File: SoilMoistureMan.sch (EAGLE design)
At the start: 21 parts, among them Q1 BC847CSMD, Q2 BC857C, Q3 BC847CSMD, Q4 BC847CSMD, Q5 BC847CSMD

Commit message: schematic and Routing changes
schematic and Routing changes still WIP
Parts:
- added BAT2: 2032, kzh20_lithium_batterie_holder:2032
- BAT1: MF (none) -> KEYSTONE; MPN (none) -> 3000; OC_FARNELL unknown -> 1650692
- D1: value SS12B -> S1A-13-F; MF (none) -> DIODES INC.; MPN (none) -> S1A-13-F; OC_FARNELL (none) -> 1858625
- F1: value (none) -> Resettable_Fuse; MF (none) -> MULTICOMP; MPN (none) -> MC36207; OC_FARNELL (none) -> 2366765
- Q2: value BC857C -> BC847CSMD; device transistor:BC857C-PNP-SOT23-BEC -> transistor-npn:BC847CSMD; MPN BC857C-7-F -> BC848C-7-F; OC_FARNELL 1773640 -> 1773621
- Q3: value BC847CSMD -> BC857C; device transistor-npn:BC847CSMD -> transistor:BC857C-PNP-SOT23-BEC; MPN BC848C-7-F -> BC857C-7-F; OC_FARNELL 1773621 -> 1773640
- R2: device resistor:R-EU_R0805 -> rcl:R-EU_R0805
- R3: value 1k -> 100k; device rcl:R-EU_R0805 -> resistor:R-EU_R0805; MPN ERJU06F1001V -> ERJ6GEYJ104V; OC_FARNELL 2145438 -> 2057731
- R4: value 1k -> 10k
- R5: value 100k -> 1k; MPN ERJ6GEYJ104V -> ERJU06F1001V; OC_FARNELL 2057731 -> 2145438
- R7: value 1k -> 100k; MPN ERJU06F1001V -> ERJ6GEYJ104V; OC_FARNELL 2145438 -> 2057731
- VR1: MF (none) -> BOURNS; MPN (none) -> TC33X-2-104E; OC_FARNELL unknown -> 1689864
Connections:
- new net N$13: Q2.C, R3.1, R4.1
- net GND: now also BAT2.-, Q2.E, Q5.E; no longer Q3.E
- net N$1: now also Q3.C, R8.2; no longer Q2.C, R4.2
- net N$10: now also Q4.B, R7.1; no longer Q3.B, R6.1
- net N$11: now also Q5.C; no longer Q4.C
- net N$12: now also Q5.B, R6.1; no longer Q4.B, R5.1
- net N$2: now also R5.1; no longer R4.1
- net N$3: now also Q3.B, R4.2; no longer Q2.B, R2.1, R3.2
- net N$4: now also Q2.B, R2.1; no longer R3.1
- net N$5: now also R8.1; no longer R7.1
- net N$6: now also Q3.E, R3.2; no longer Q2.E
- net N$7: now also Q4.C; no longer Q3.C
- net VCC: now also BAT2.+
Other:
- note added: "ONLY 1 BATTERY FITTED"
- moved on the sheet: BAT1, C1, C2, D1, F1, LED1, LED2, Q4, Q5, R2, R3, R4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

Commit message: Layout changes and Bat 2 changed to bat 1
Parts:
- removed BAT2: 2032, kzh20_lithium_batterie_holder:2032
- BAT1: value CR1220SMD -> 2032; device adafruit:CR1220SMT -> kzh20_lithium_batterie_holder:2032; MF KEYSTONE -> RENATA; MPN 3000 -> SMTU 2032-LF; OC_FARNELL 1650692 -> 1216354
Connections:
- net GND: no longer BAT2.-
- net VCC: no longer BAT1.+1, BAT2.+
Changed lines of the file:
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@@
 <attribute name="OC_FARNELL" value="2346364"/>
-</part>
-<part name="BAT1" library="adafruit" deviceset="CR1220" device="SMT" value="CR1220SMD">
-<attribute name="MF" value="KEYSTONE"/>
-<attribute name="MPN" value="3000"/>
-<attribute name="OC_FARNELL" value="1650692"/>
 </part>
 <part name="SUPPLY1" library="supply2" deviceset="GND" device=""/>
@@
 <attribute name="OC_FARNELL" value="2145438"/>
 </part>
-<part name="BAT2" library="kzh20_lithium_batterie_holder" deviceset="2032" device="">
+<part name="BAT1" library="kzh20_lithium_batterie_holder" deviceset="2032" device="">
 <attribute name="MF" value="RENATA"/>
 <attribute name="MPN" value="SMTU 2032-LF"/>
@@
 <attribute name="MPN" x="109.22" y="66.04" size="1.778" layer="96" display="off"/>
 </instance>
-<instance part="BAT1" gate="G$1" x="-48.26" y="71.12" rot="R90">
-<attribute name="OC_FARNELL" x="-48.26" y="71.12" size="1.778" layer="96" display="off"/>
-<attribute name="MF" x="-48.26" y="71.12" size="1.778" layer="96" display="off"/>
-<attribute name="MPN" x="-48.26" y="71.12" size="1.778" layer="96" display="off"/>
-</instance>
 <instance part="SUPPLY1" gate="GND" x="91.44" y="30.48"/>
 <instance part="LED1" gate="G$1" x="66.04" y="73.66">
@@
 <attribute name="MPN" x="53.34" y="76.2" size="1.778" layer="96" display="off"/>
 </instance>
-<instance part="BAT2" gate="G$1" x="-60.96" y="76.2" rot="R90">
+<instance part="BAT1" gate="G$1" x="-60.96" y="76.2" rot="R90">
 <attribute name="OC_FARNELL" x="-60.96" y="76.2" size="1.778" layer="96" display="off"/>
 <attribute name="MF" x="-60.96" y="76.2" size="1.778" layer="96" display="off"/>
@@
 </segment>
 <segment>
-<pinref part="BAT1" gate="G$1" pin="-"/>
 <pinref part="D1" gate="G$1" pin="A"/>
-<wire x1="-48.26" y1="60.96" x2="-48.26" y2="66.04" width="0.1524" layer="91"/>
 <wire x1="-17.78" y1="73.66" x2="-17.78" y2="60.96" width="0.1524" layer="91"/>
 <wire x1="-17.78" y1="60.96" x2="-35.56" y2="60.96" width="0.1524" layer="91"/>
-<junction x="-48.26" y="60.96"/>
-<pinref part="BAT2" gate="G$1" pin="-"/>
-<wire x1="-35.56" y1="60.96" x2="-48.26" y2="60.96" width="0.1524" layer="91"/>
+<pinref part="BAT1" gate="G$1" pin="-"/>
 <wire x1="-60.96" y1="71.12" x2="-60.96" y2="60.96" width="0.1524" layer="91"/>
-<wire x1="-60.96" y1="60.96" x2="-48.26" y2="60.96" width="0.1524" layer="91"/>
+<wire x1="-60.96" y1="60.96" x2="-35.56" y2="60.96" width="0.1524" layer="91"/>
 <pinref part="SUPPLY2" gate="GND" pin="GND"/>
 <wire x1="-35.56" y1="55.88" x2="-35.56" y2="60.96" width="0.1524" layer="91"/>
@@
 <net name="VCC" class="0">
 <segment>
-<wire x1="-48.26" y1="91.44" x2="-43.18" y2="91.44" width="0.1524" layer="91"/>
-<junction x="-48.26" y="91.44"/>
-<wire x1="-48.26" y1="78.74" x2="-48.26" y2="91.44" width="0.1524" layer="91"/>
-<pinref part="BAT1" gate="G$1" pin="+1"/>
-<wire x1="-45.72" y1="76.2" x2="-45.72" y2="78.74" width="0.1524" layer="91"/>
-<wire x1="-45.72" y1="78.74" x2="-48.26" y2="78.74" width="0.1524" layer="91"/>
-<junction x="-48.26" y="78.74"/>
-<wire x1="-50.8" y1="78.74" x2="-48.26" y2="78.74" width="0.1524" layer="91"/>
+<pinref part="F1" gate="G$1" pin="1"/>
 <pinref part="BAT1" gate="G$1" pin="+"/>
-<wire x1="-50.8" y1="76.2" x2="-50.8" y2="78.74" width="0.1524" layer="91"/>
-<pinref part="F1" gate="G$1" pin="1"/>
-<pinref part="BAT2" gate="G$1" pin="+"/>
 <wire x1="-60.96" y1="81.28" x2="-60.96" y2="91.44" width="0.1524" layer="91"/>
-<wire x1="-60.96" y1="91.44" x2="-48.26" y2="91.44" width="0.1524" layer="91"/>
+<wire x1="-60.96" y1="91.44" x2="-43.18" y2="91.44" width="0.1524" layer="91"/>
 <pinref part="P+1" gate="VCC" pin="VCC"/>
 <wire x1="-60.96" y1="96.52" x2="-60.96" y2="91.44" width="0.1524" layer="91"/>

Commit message: CAD B Commit
CAD B Commit - used to produce CAD B boards
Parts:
- removed Q5: BC847CSMD, transistor-npn:BC847CSMD
- C1: value 100uF -> 1uF; device rcl:CPOL-EUSANYO_SMD_C6 -> resistor:C-EUC0603; MF RUBYCON -> MURATA; MPN 25TZV100M6.3X8 -> GRM188R61A105MA61D; OC_FARNELL 2346375 -> 2362096
- C2: value 10uF -> 100nF; device rcl:CPOL-EUSANYO_SMD_C6 -> resistor:C-EUC0603; MF RUBYCON -> MULTICOMP; MPN 16TZV10M4X6.1 -> MC0603B104M160CT; OC_FARNELL 2346364 -> 1709956
- D1: value S1A-13-F -> 0.5A SOD-323; device diode:DIODE-SMB -> adafruit:DIODESOD-323F; MF DIODES INC. -> NXP; MPN S1A-13-F -> PMEG3010EJ,115; OC_FARNELL 1858625 -> 1757770
- F1: value Resettable_Fuse -> 100MA PTC FUSE; device adafruit:PTCFUSE-1206 -> rcl:R-EU_R0805; MF MULTICOMP -> BOURNS; MPN MC36207 -> MF-PSMF010X-2; OC_FARNELL 2366765 -> 1294873
- LED1, LED2: value GENERIC_0805_SMD_LED -> GENERIC_0603_SMD_LED; device led:LEDCHIPLED_0805 -> led:LEDSML0603; MF LUMEX -> AVAGO TECHNOLOGIES; MPN SML-LX1206SRW-TR -> ASMT-CR00; OC_FARNELL 2062242 -> 1863233
- Q1, Q4: MPN BC848C-7-F -> BC847C-7-F; OC_FARNELL 1773621 -> 1773609
- Q2: value BC847CSMD -> BC857C; device transistor-npn:BC847CSMD -> transistor:BC857C-PNP-SOT23-BEC; MPN BC848C-7-F -> BC857C-7-F; OC_FARNELL 1773621 -> 1773640
- Q3: value BC857C -> BC847CSMD; device transistor:BC857C-PNP-SOT23-BEC -> transistor-npn:BC847CSMD; MPN BC857C-7-F -> BC847C-7-F; OC_FARNELL 1773640 -> 1773609
- R1: value 20k -> 150k; device resistor:R-EU_R0805 -> resistor:R-EU_R0603; MF PANASONIC -> MULTICOMP; MPN ERJ6GEYJ203V -> MC0063W06031150K; OC_FARNELL 2057722 -> 1127417
- R2: value 100k -> 1Meg; device rcl:R-EU_R0805 -> resistor:R-EU_R0603; MF PANASONIC -> YAGEO; MPN ERJ6GEYJ104V -> RC0603JR-071ML; OC_FARNELL 2057731 -> 1799380
- R3: value 100k -> 10k; device resistor:R-EU_R0805 -> resistor:R-EU_R0603; MF PANASONIC -> YAGEO; MPN ERJ6GEYJ104V -> RC0603JR-1010KL; OC_FARNELL 2057731 -> 1799457
- R4: value 10k -> 1Meg; device rcl:R-EU_R0805 -> resistor:R-EU_R0603; MF PANASONIC -> YAGEO; MPN ERJU06F1001V -> RC0603JR-071ML; OC_FARNELL 2145438 -> 1799380
- R5: value 1k -> 10Meg; device rcl:R-EU_R0805 -> resistor:R-EU_R0603; MF PANASONIC -> MULTICOMP; MPN ERJU06F1001V -> MC0063W0603110M0; OC_FARNELL 2145438 -> 2141628RL
- R6: value 100k -> 10Meg; device rcl:R-EU_R0805 -> resistor:R-EU_R0603; MF PANASONIC -> MULTICOMP; MPN ERJ6GEYJ104V -> MC0063W0603110M0; OC_FARNELL 2057731 -> 2141628RL
- R7: value 100k -> 2k; device rcl:R-EU_R0805 -> resistor:R-EU_R0603; MF PANASONIC -> YAGEO; MPN ERJ6GEYJ104V -> RC0603JR-072KL; OC_FARNELL 2057731 -> 1799398
- R8: value 1k -> 0R0; device rcl:R-EU_R0805 -> resistor:R-EU_R0603; MF PANASONIC -> MULTICOMP; MPN ERJU06F1001V -> MC0603SAF0000T5E; OC_FARNELL 2145438 -> 2309111
- VR1: MPN TC33X-2-104E -> 3314J-1-104E; OC_FARNELL 1689864 -> 514792RL
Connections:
- removed net N$4: Q1.C, Q2.B, R2.1
- removed net N$6: D1.C, F1.2, Q3.E, R1.2, R2.2, R3.2
- removed net SOIL_PROBE_B: Q1.B, VR1.E
- new net N$9: R1.2, VR1.S
- new net VCC_FUSED: D1.C, F1.2, Q2.E, R2.2, VR1.E
- net GND: now also Q3.E; no longer Q2.E, Q5.E, VR1.S
- net N$1: now also Q2.C, R4.2; no longer Q3.C, R8.2
- net N$10: now also C2.1, Q3.B, R6.1; no longer C2.-, Q4.B, R7.1
- net N$11: now also C2.2, LED1.C, Q4.C; no longer C2.+, Q5.C
- net N$12: now also C1.2, Q4.B, R5.1; no longer C1.-, Q5.B, R6.1
- net N$13: now also Q1.C, R2.1; no longer Q2.C, R4.1
- net N$2: now also R4.1, R8.2; no longer LED1.A, R5.1
- net N$3: now also Q2.B, R3.2; no longer Q3.B, R4.2
- net N$5: now also LED1.A, R7.1; no longer R8.1
- net N$7: now also C1.1, Q3.C, R8.1; no longer C1.+, LED1.C, Q4.C
- net SOIL_PROBE_A: now also Q1.B
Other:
- note added: "Check parts against final footprints and against bom. Parts here are not final. The part values have changed. the orderable parts need updating!!!!"
- note removed: "Check parts against final footprints and against bom. Parts here are not final."
- note removed: "ONLY 1 BATTERY FITTED"
- moved on the sheet: LED1, LED2, Q4, R1, R2, R3, R4, R5, R6, R7, R8, VR1

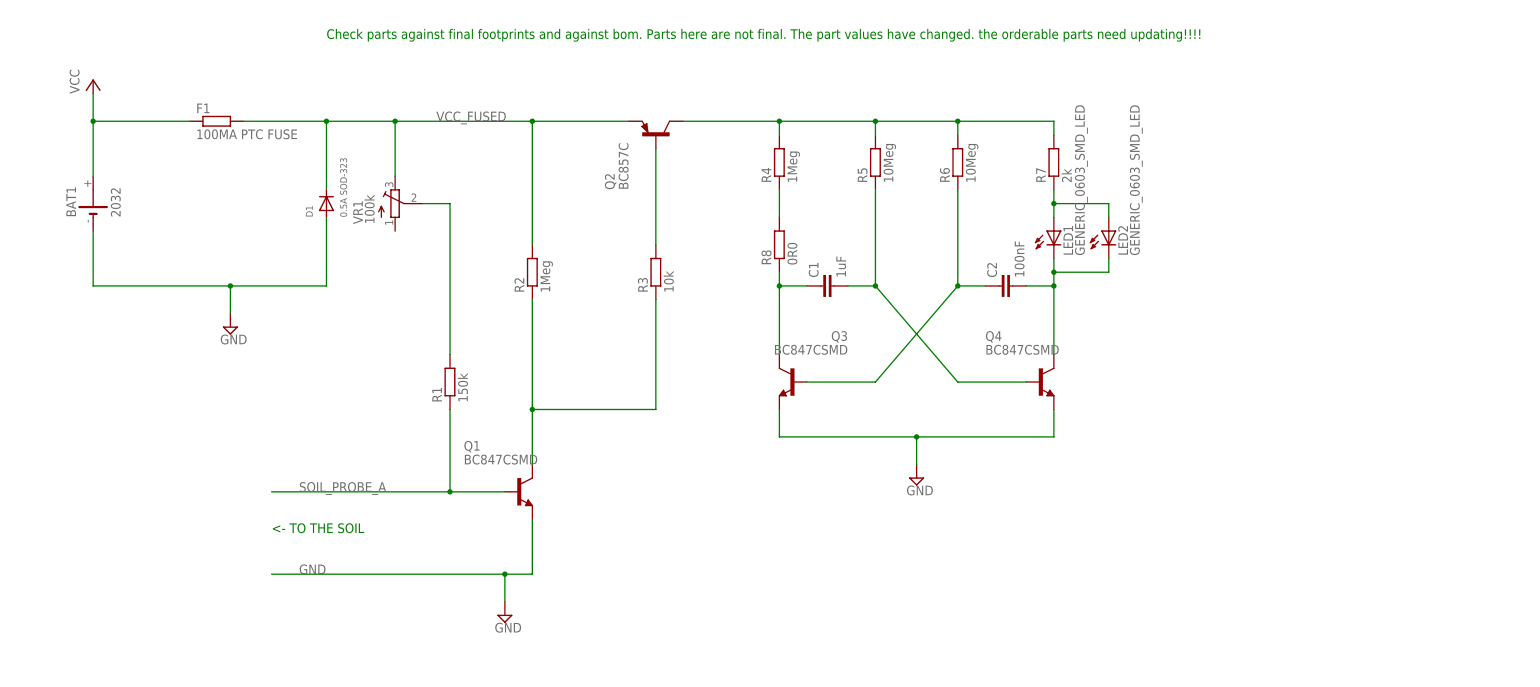
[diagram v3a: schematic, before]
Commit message: First CAD C commit
Updated one resistor value from 1MOhm to 100k. added warning text about
electrolysis to pcb and another to the schematic
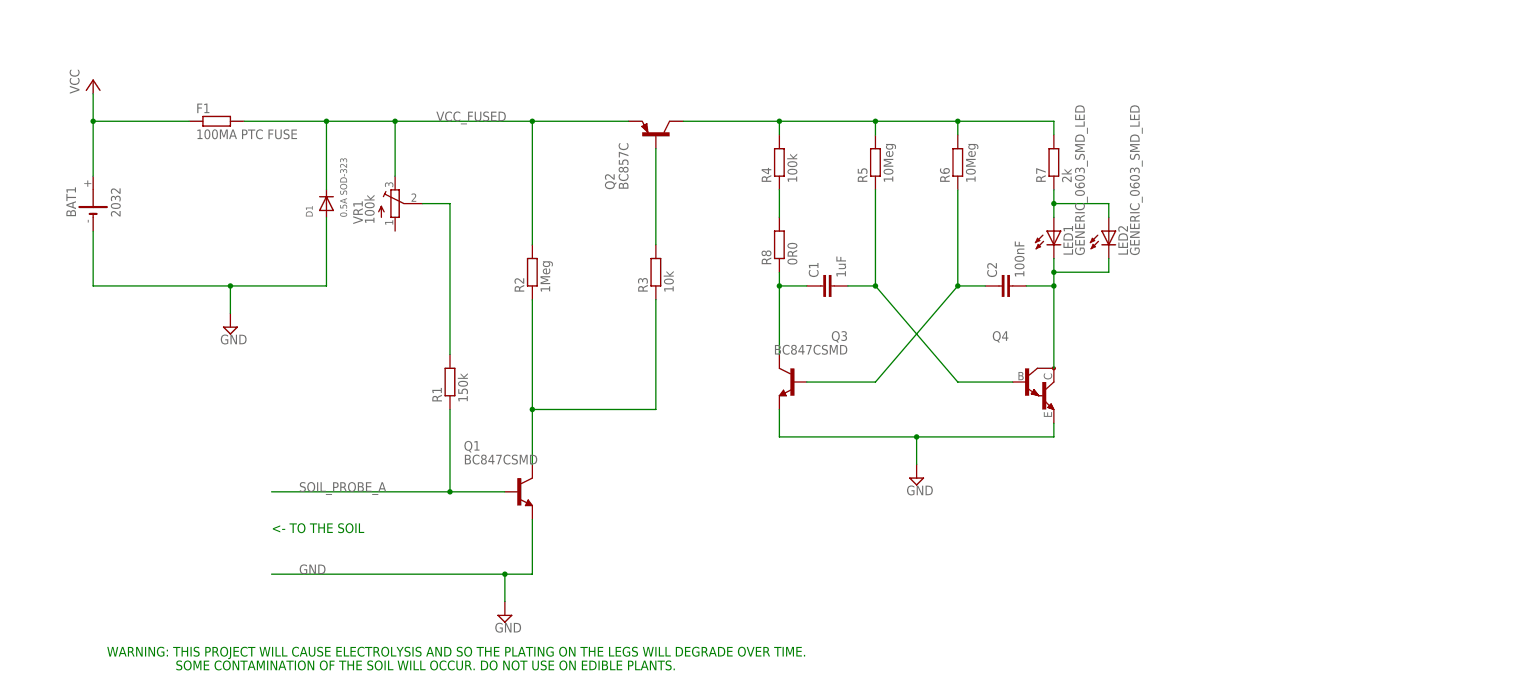
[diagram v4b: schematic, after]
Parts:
- C1: MF MURATA -> TDK; MPN GRM188R61A105MA61D -> C1608X5R1C105K080AA; OC_FARNELL 2362096 -> 2211167
- C2: MPN MC0603B104M160CT -> MC0603B104K160CT; OC_FARNELL 1709956 -> 1759016
- Q4: value BC847CSMD -> MMBTA13LT1; device transistor-npn:BC847CSMD -> transistor-npn:MMBTA13LT1; MF DIODES INC. -> FAIRCHILD SEMICONDUCTOR; MPN BC847C-7-F -> BCV27; OC_FARNELL 1773609 -> 9846689
- R1: MF MULTICOMP -> TE CONNECTIVITY; MPN MC0063W06031150K -> CRGH0603J150K; OC_FARNELL 1127417 -> 2331756
- R2: MF YAGEO -> TE CONNECTIVITY; MPN RC0603JR-071ML -> CRGH0603J1M0; OC_FARNELL 1799380 -> 2331766
- R3: MF YAGEO -> BOURNS; MPN RC0603JR-1010KL -> CR0603-JW-103GLF; OC_FARNELL 1799457 -> 2333522
- R4: value 1Meg -> 100k; MF YAGEO -> TE CONNECTIVITY; MPN RC0603JR-071ML -> CRGH0603J100K; OC_FARNELL 1799380 -> 2331753
- R5, R6: OC_FARNELL 2141628RL -> 2141628
- R7: MF YAGEO -> TE CONNECTIVITY / NEOHM; MPN RC0603JR-072KL -> CPF0603F2K0C1; OC_FARNELL 1799398 -> 1527506
- VR1: MF BOURNS -> VISHAY SFERNICE; MPN 3314J-1-104E -> TS53YJ104MR10; OC_FARNELL 514792RL -> 1141488
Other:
- note added: "SOME CONTAMINATION OF THE SOIL WILL OCCUR. DO NOT USE ON EDIBLE PLANTS."
- note added: "WARNING: THIS PROJECT WILL CAUSE ELECTROLYSIS AND SO THE PLATING ON THE LEGS WILL DEGRADE OVER TIME."
- note removed: "Check parts against final footprints and against bom. Parts here are not final. The part values have changed. the orderable parts need updating!!!!"
